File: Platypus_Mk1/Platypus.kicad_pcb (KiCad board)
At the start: 4 copper layers, 75 x 57 mm, 63 parts, among them CN1 SERVO_PWM, CN10 FEMALE_LEFT, CN11 FEMALE_RIGHT, CN2 CFG1, CN3 CFG1, CN4 CFG1, CN5 FEMALE_LEFT, CN6 FEMALE_RIGHT, CN7 CFG1, CN8 CFG1, CN9 CFG1, J1 PJ-202AH, J10 ICSP, J11 MotorTerm, J12 MotorHeader, J13 MotorTerm, J14 MotorHeader, J15 12V_TERM, J2 TermLaser, J3 TermStop, J4 LASER_PWR, J5 LASER_PULSE, J6 TermControl, J7 TermLimit, J8 TermAux, J9 UJ2-BH-1-TH, K1 SW_RESET, U1 CJ7805, U2 INTERFACE-CH340T_SSOP20_, U3 MCU-ATMEGA328P-AU_TQFP32_, Y1 12MHz, Y2 16MHZ

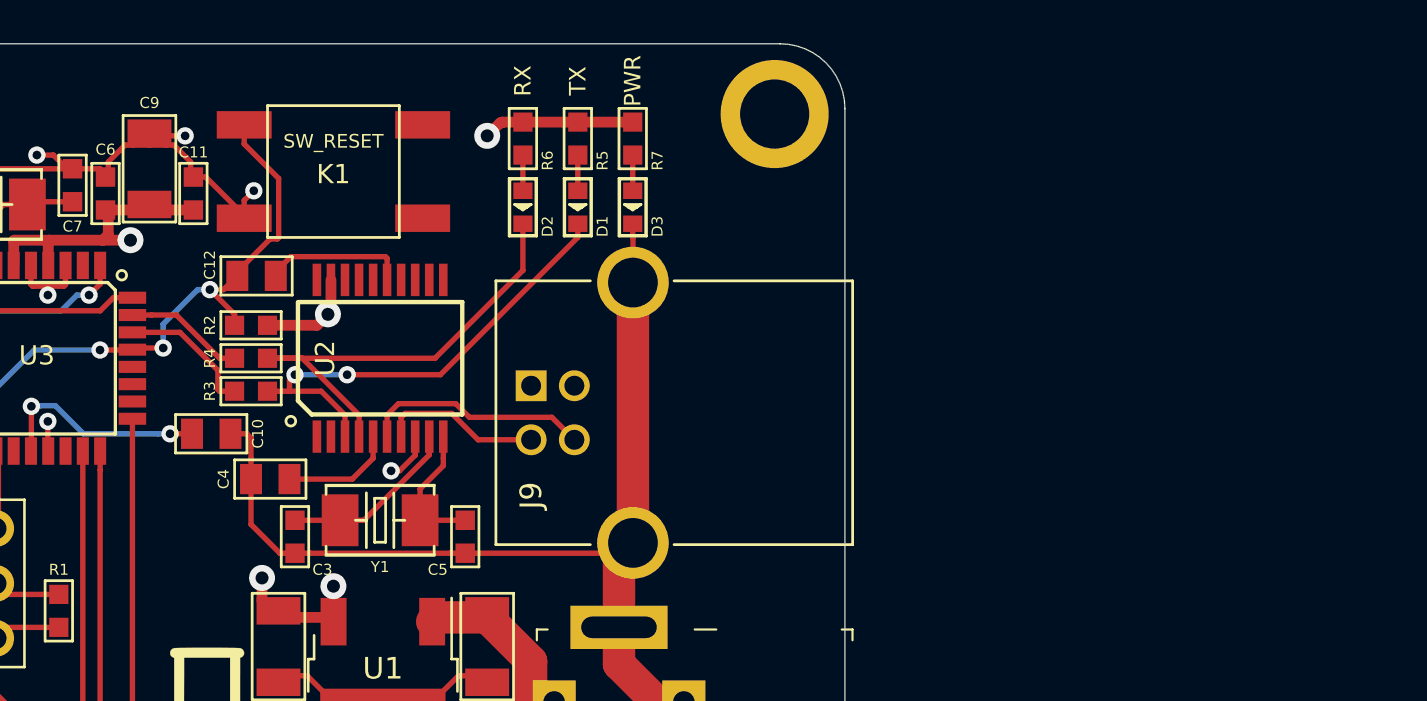
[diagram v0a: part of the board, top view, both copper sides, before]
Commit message: Change RX/TX LEDs. Add new laser conn
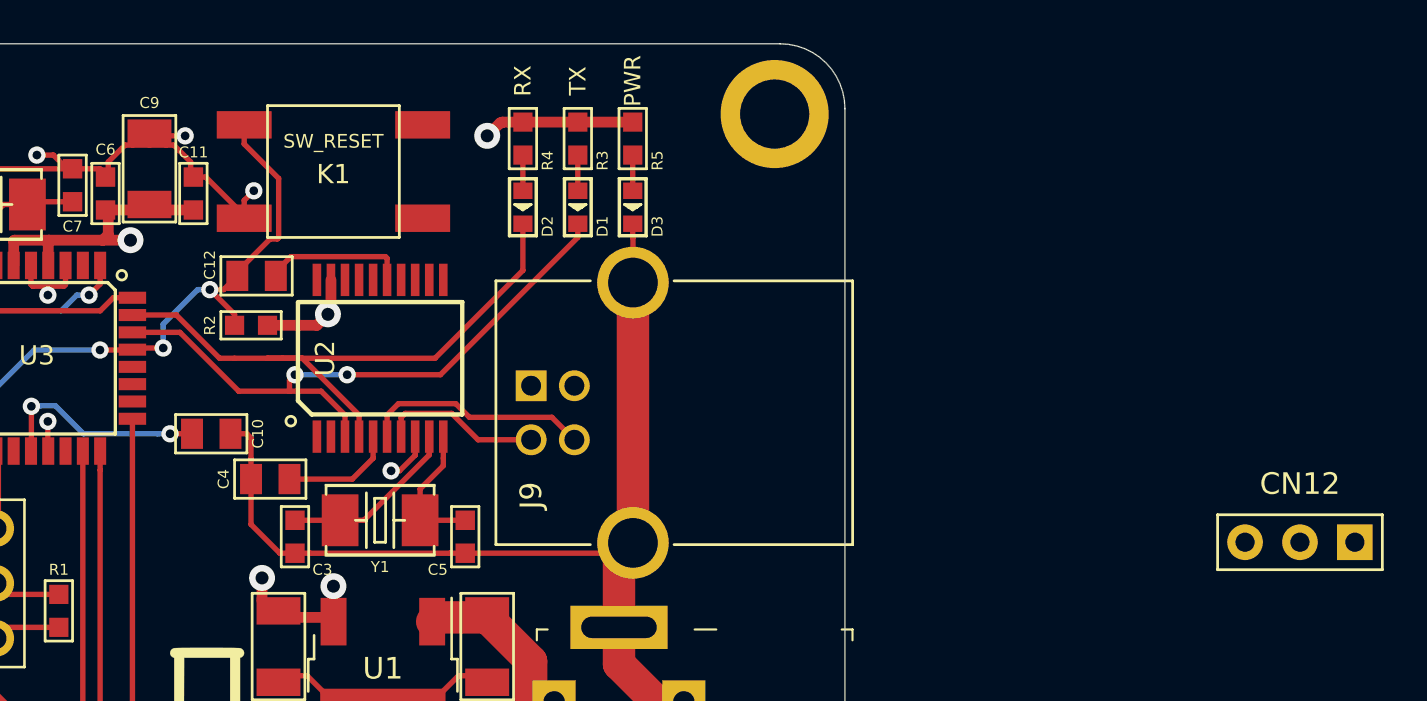
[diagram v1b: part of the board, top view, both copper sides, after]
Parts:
- removed the R5 at (207.6, 32.4)
- removed R6: 220R, OPL_Resistor:R0603
- added CN12: LASER_CONN, OPL_Connector:H3-2.54, F.Cu at (241.0, 51.1)
- D1, D2, D3: value LED_BLUE -> LED_RED
- R5: renamed from R7; value 220R -> 1K
- moved R3 19.1 mm to (207.6, 32.4), turned to 90 degrees
- moved R4 16.2 mm to (205.1, 32.4), turned to 270 degrees
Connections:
- D1 pad 2: /Arduino Nano/USB_TX -> /GRBL_RX
- D2 pad 2: /Arduino Nano/USB_RX -> /GRBL_TX
- R3 pad 1: /GRBL_RX -> Net-(D1-Pad1)
- R3 pad 2: /Arduino Nano/USB_TX -> 5V
- R4 pad 1: /GRBL_TX -> 5V
- R4 pad 2: /Arduino Nano/USB_RX -> Net-(D2-Pad1)
- U2 pad 3: /Arduino Nano/USB_TX -> /GRBL_RX
- U2 pad 4: /Arduino Nano/USB_RX -> /GRBL_TX
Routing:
- net /GRBL_TX: track 5.55 -> 29.1 mm
- net /GRBL_RX: track 6.37 -> 29.6 mm, vias 0 -> 2
- net /Arduino Nano/USB_TX: track 22.3 -> 0.00 mm, vias 2 -> 0
- net /Arduino Nano/USB_RX: track 22.0 -> 0.00 mm

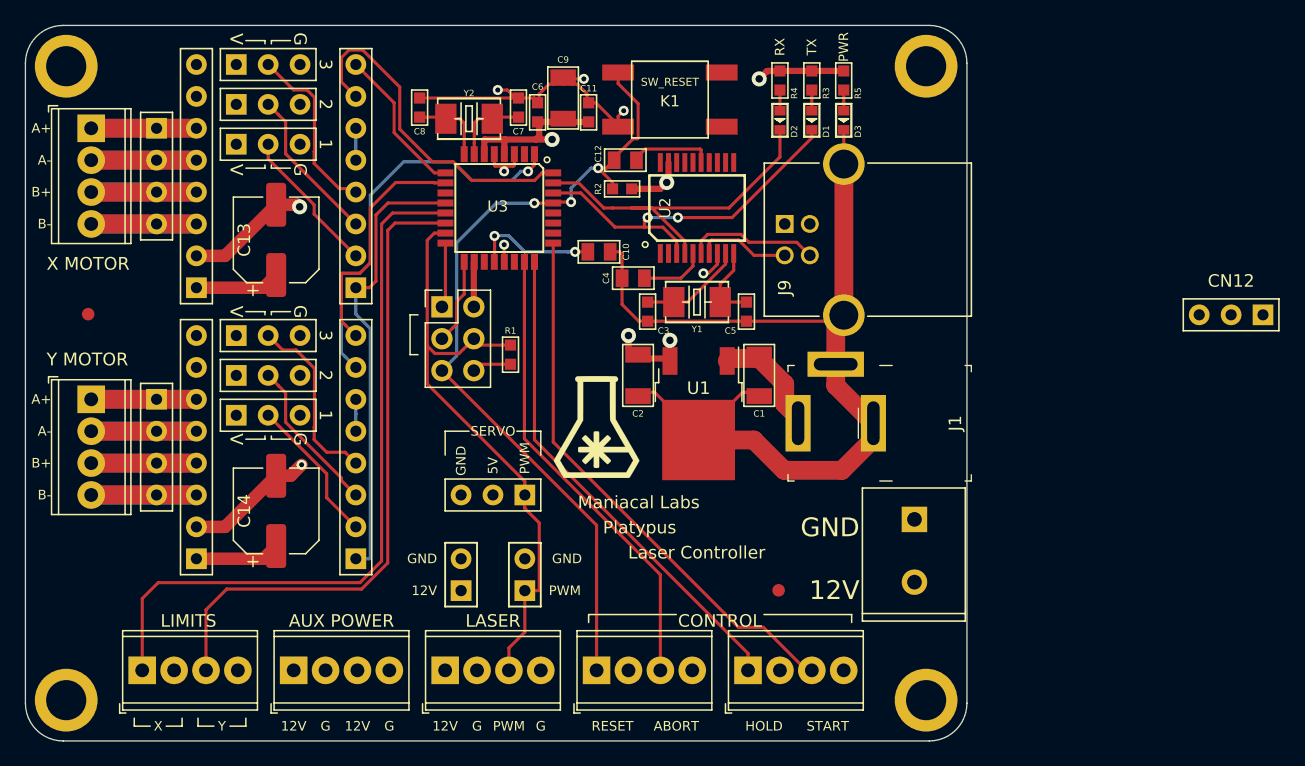
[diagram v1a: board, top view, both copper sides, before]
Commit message: rework for component moves
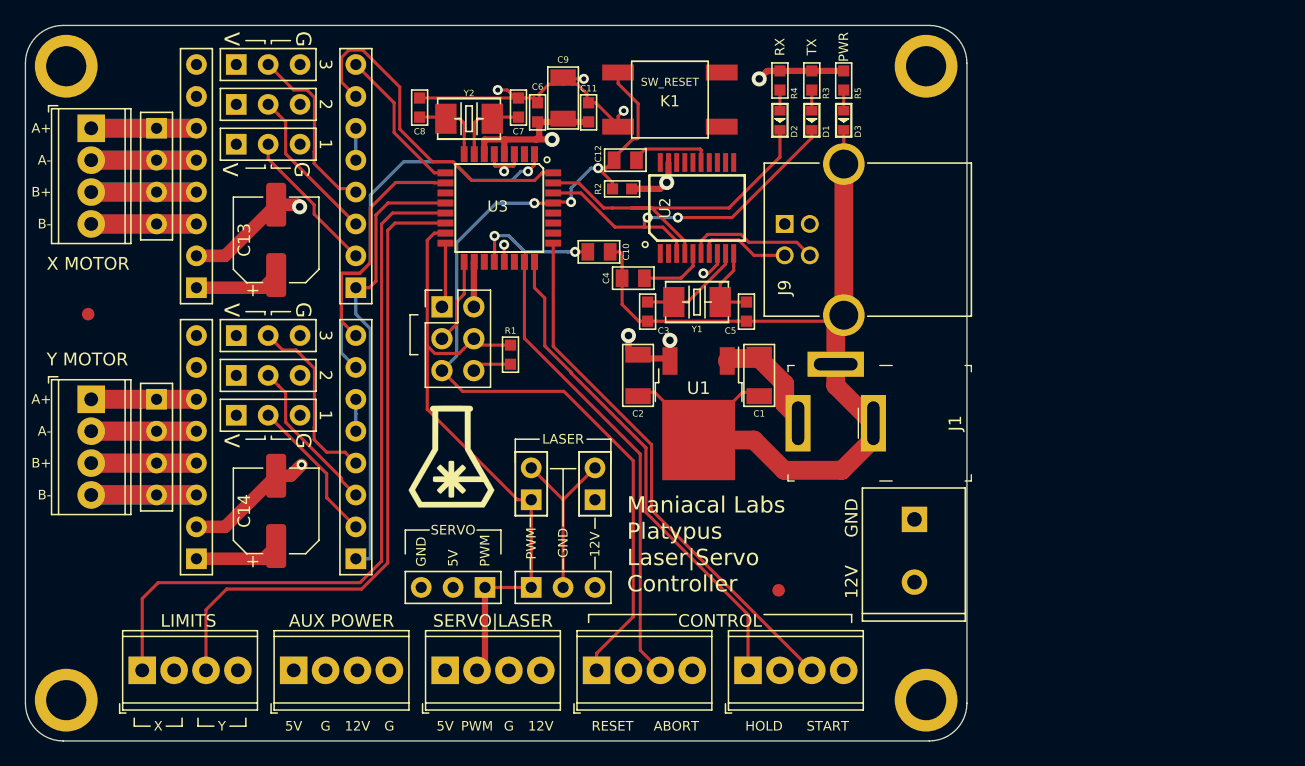
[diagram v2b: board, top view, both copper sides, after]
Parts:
- moved CN12 57.5 mm to (187.8, 72.8), turned to 180 degrees
- moved J4 12.9 mm to (190.4, 64.5)
- moved G*** 11.8 mm to (178.9, 62.4)
- moved CN1 8.02 mm to (179.1, 72.8)
- moved J5 7.26 mm to (185.3, 64.5)
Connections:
- J2 pad 1: /VIN_12V -> 5V
- J2 pad 2: GND -> /PULSE
- J2 pad 3: /PULSE -> GND
- J2 pad 4: GND -> /VIN_12V
- J8 pad 1: /VIN_12V -> 5V
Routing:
- net /VIN_12V: track 149.8 -> 228.2 mm
- net 5V: track 170.4 -> 199.6 mm
- net GND: track 542.9 -> 550.6 mm
- net /NANO_RESET: track 66.3 -> 73.5 mm
- net /PULSE: track 48.9 -> 51.5 mm
- net /START: track 44.0 -> 42.6 mm
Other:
- board text added: "Maniacal Labs Platypus Laser|Servo Controller"
- board text added: "SERVO|LASER"
- board text removed: "Laser Controller"
- board text removed: "Maniacal Labs"
- board text removed: "Platypus"

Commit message: Adding platypus graphic
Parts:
- added G***: LOGO, LOGOS:platypus, B.Cu at (195.1, 52.3)
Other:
- board text added: "ManiacalLabs.com/Platypus"
